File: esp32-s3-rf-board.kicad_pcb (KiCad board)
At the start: 4 copper layers, 50 x 40 mm, 26 parts, among them J1 USB-C 16P, J2 u.FL, J3 UART_4P, J4 I2C_4P, J5 SPI_6P, SW1 RST_BTN, SW2 BOOT_BTN, U1 ESP32-S3-WROOM, U2 AP2112K-3.3V, U3 CP2102-GMR

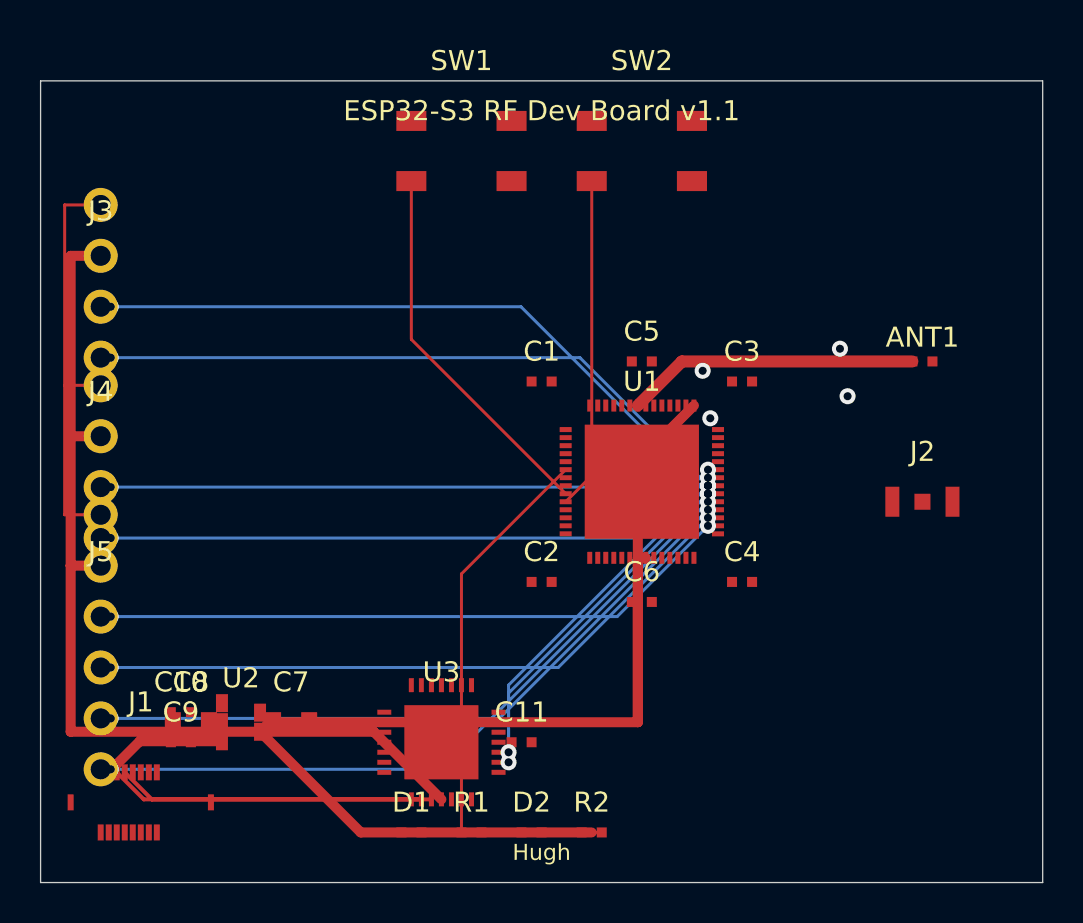
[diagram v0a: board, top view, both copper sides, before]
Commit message: v1.2: 40 MHz crystal, ESP32-S3FN8 flash, real schematic
Closes the three fab-blockers for the bare QFN56 design. Adds Y1
(40 MHz NX3225GA) with C12/C13 12 pF NP0 load caps on XTAL_P/XTAL_N,
swaps U1 to ESP32-S3FN8 (8 MB internal flash, same QFN56 footprint),
and replaces the placeholder .kicad_sch with real symbols + nets
(ERC: 0 errors). Also adds EN 10k pull-up (R5), USB 22R series damping
(R6, R7), decaps repositioned within 2 mm of every VDD pad, and the
previously-uncommitted v1.1 USB-C CC / ESD / test-point work in
reroute_clean.py.

Layout cleanup still pending: the auto-generator leaves 135 DRC
violations and 122 unconnected nets (USB-C pads overlapping J5, LDO
near C8, RF keepout around antenna). Manual Pcbnew pass required
before sending Gerbers to JLCPCB.
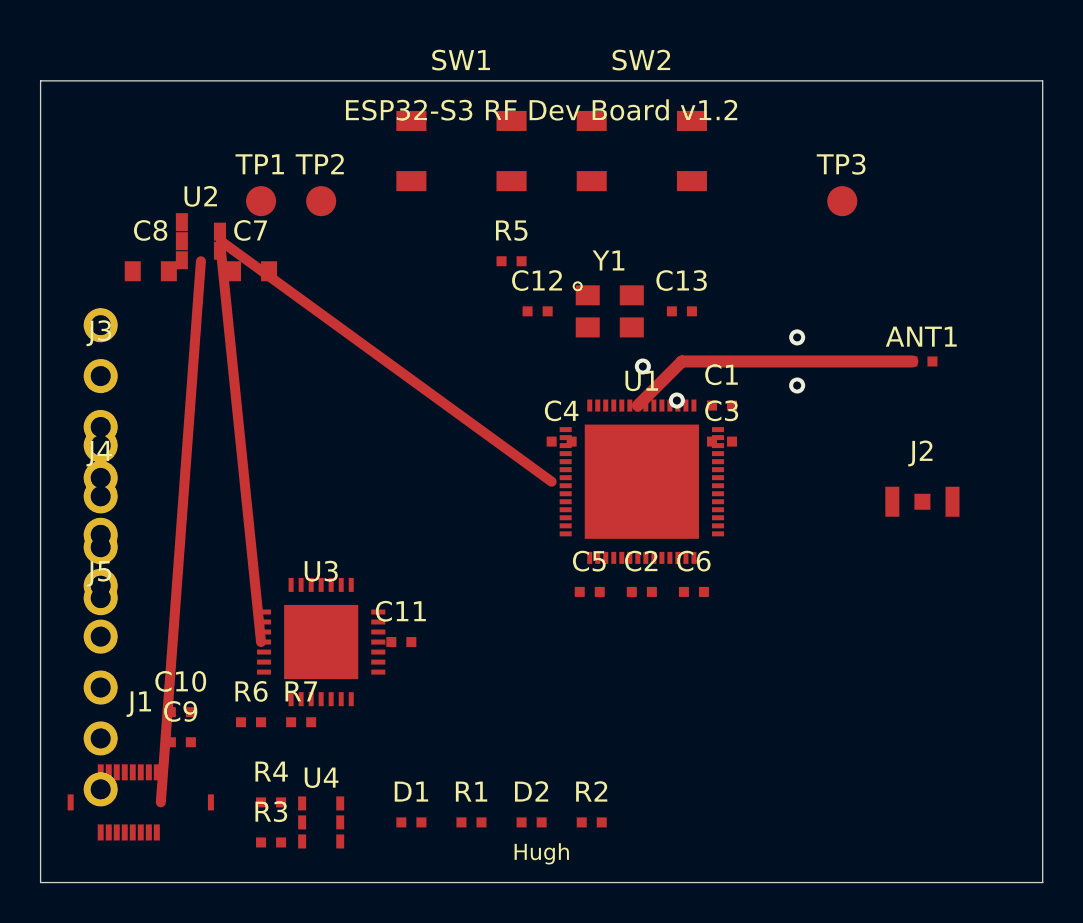
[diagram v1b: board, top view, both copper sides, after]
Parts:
- added C12: 12pF, C12_fp, F.Cu at (24.8, 11.5)
- added C13: 12pF, C13_fp, F.Cu at (32.0, 11.5)
- added R3: 5.1k, R3_fp, F.Cu at (11.5, 38.0)
- added R4: 5.1k, R4_fp, F.Cu at (11.5, 36.0)
- added R5: 10k, R5_fp, F.Cu at (23.5, 9.00)
- added R6: 22R, R6_fp, F.Cu at (10.5, 32.0)
- added R7: 22R, R7_fp, F.Cu at (13.0, 32.0)
- added TP1: TP_3V3, TP1_fp, F.Cu at (11.0, 6.00)
- added TP2: TP_GND, TP2_fp, F.Cu at (14.0, 6.00)
- added TP3: TP_RF, TP3_fp, F.Cu at (40.0, 6.00)
- added U4: USBLC6-2SC6, U4_fp, F.Cu at (14.0, 37.0)
- added Y1: 40MHz, Y1_fp, F.Cu at (28.4, 11.5)
- moved U2 24.1 mm to (8.00, 8.00)
- moved C7 22.6 mm to (10.5, 9.50)
- moved C8 22.6 mm to (5.50, 9.50)
- moved C5 11.8 mm to (27.4, 25.5)
- moved C4 11.4 mm to (26.0, 18.0)
- moved C1 9.08 mm to (34.0, 16.2)
- moved C11 7.81 mm to (18.0, 28.0)
- moved U3 7.81 mm to (14.0, 28.0)
- moved J3 6.00 mm to (3.00, 16.0)
- moved C2 5.02 mm to (30.0, 25.5)
- moved C3 3.16 mm to (34.0, 18.0)
- moved J4 3.00 mm to (3.00, 22.0)
- moved C6 2.65 mm to (32.6, 25.5)
- moved J5 1.00 mm to (3.00, 29.0)
- moved D1 0.50 mm to (18.5, 37.0)
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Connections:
- J1 pad 13: (no net) -> USB_CC2
- J1 pad 5: (no net) -> USB_CC1
- U1 pad 24: (no net) -> I2C_SDA
- U1 pad 25: (no net) -> I2C_SCL
- U1 pad 39: (no net) -> XTAL_P
- U1 pad 40: (no net) -> XTAL_N
- U3 pad 2: USB_DM -> USB_DM_CP
- U3 pad 3: USB_DP -> USB_DP_CP
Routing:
- net 3V3: track 111.4 -> 40.0 mm
- net UART_TX: track 53.2 -> 0.00 mm, vias 4 -> 0
- net UART_RX: track 51.9 -> 0.00 mm, vias 4 -> 0
- net SPI_CS: track 36.3 -> 0.00 mm, vias 2 -> 0
- net SPI_SCK: track 35.1 -> 0.00 mm, vias 2 -> 0
- net SPI_MISO: track 33.9 -> 0.00 mm, vias 2 -> 0
- net SPI_MOSI: track 32.7 -> 0.00 mm, vias 2 -> 0
- net I2C_SCL: track 32.2 -> 0.00 mm, vias 2 -> 0
- net I2C_SDA: track 31.0 -> 0.00 mm, vias 2 -> 0
- net GND: track 20.9 -> 0.00 mm
- net 5V: track 6.29 -> 27.1 mm
- net GPIO48_LED: track 20.3 -> 0.00 mm
- net EN: track 18.8 -> 0.00 mm
- net GPIO0: track 16.5 -> 0.00 mm
- net USB_DP: track 15.9 -> 0.00 mm
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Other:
- board text added: "ESP32-S3 RF Dev Board v1.2"
- board text removed: "ESP32-S3 RF Dev Board v1.1"

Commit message: v1.2: programmatic DRC cleanup -- 144 -> 33 violations, 0 shorts
Fix the structural issues left over from the auto-generator:

- RF trace: narrow fanout from pad 36 (0.25 mm) widening to 0.6 mm once
  clear of adjacent top-row pads, then vertical stub -> 45-deg -> horizontal.
- RF keepout on F.Cu relaxed to copperpour-only (antenna pads and feed
  trace now allowed; In1.Cu and B.Cu still fully blocked).
- Stitching vias: bumped perpendicular offset 1.2 -> 1.8 mm, dropped the
  chip-adjacent segment, skipped vias inside the 5 mm antenna keepout.
- Removed the long diagonal surface power traces from USB-C/LDO that
  cut through unrelated pads; power distribution now relies on the 3V3
  inner plane + short stubs (to be routed in Pcbnew).
- Relocated footprints: USB-C to (25, 37) so J5 SPI header no longer
  overlaps its pads; headers spread to J3=y6, J4=y17, J5=(8, 25) so no
  THT pad pair is within 1.7 mm; C8 moved off U2 pad 3; C11 offset
  right of U3 pad 11; decaps C3/C4 moved clear of U1 pads 26/27/44/45.
- SOT-23-5 pad 0.6x0.9 -> 0.55x0.8 so intra-footprint clearance passes
  the 0.1 mm rule.
- POWER netclass clearance 0.15 -> 0.1 mm (matches default).
- allow_soldermask_bridges_in_footprints: yes.

Final state: 0 shorts, 0 clearance, 0 keepout, 0 hole-clearance errors.
Remaining 33 are courtyard/silk/dangling-via warnings. 120 unconnected
nets still need a Pcbnew routing pass before Gerber export.
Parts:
- moved C10 20.0 mm to (27.0, 32.5)
- moved C9 20.0 mm to (27.0, 34.0)
- moved J1 20.0 mm to (25.0, 37.0)
- moved D1 20.0 mm to (38.5, 37.0)
- moved R1 20.0 mm to (41.5, 37.0)
- moved D2 19.0 mm to (43.5, 37.0)
- moved R2 19.0 mm to (46.5, 37.0)
- moved R4 18.5 mm to (30.0, 35.0)
- moved J3 10.0 mm to (3.00, 6.00)
- moved R3 9.01 mm to (20.0, 35.0)
- moved J5 6.40 mm to (8.00, 25.0)
- moved J4 5.00 mm to (3.00, 17.0)
- moved U4 4.00 mm to (18.0, 37.0)
- moved C8 2.06 mm to (6.00, 11.5)
- moved C3 1.50 mm to (35.5, 18.0)
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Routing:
- net 3V3: track 40.0 -> 0.00 mm
- net 5V: track 27.1 -> 0.00 mm
- net RF_ANT: track 14.6 -> 15.5 mm
- net GND: vias 4 -> 2
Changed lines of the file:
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@@
     (pad_to_mask_clearance 0.05)
     (solder_mask_min_width 0.05)
-    (allow_soldermask_bridges_in_footprints no)
+    (allow_soldermask_bridges_in_footprints yes)
     (pcbplotparams
       (layerselection 0x00010fc_ffffffff)
@@
     (fp_line (start 1.5 1.4) (end -1.5 1.4) (layer "F.Fab") (stroke (width 0.1) (type solid)))
     (fp_line (start -1.5 1.4) (end -1.5 -1.4) (layer "F.Fab") (stroke (width 0.1) (type solid)))
-    (pad "1" smd rect (at -0.95 -0.95) (size 0.6 0.9) (layers "F.Cu" "F.Paste" "F.Mask") (net 16 "EN"))
-    (pad "2" smd rect (at -0.95 0) (size 0.6 0.9) (layers "F.Cu" "F.Paste" "F.Mask") (net 1 "GND"))
-    (pad "3" smd rect (at -0.95 0.95) (size 0.6 0.9) (layers "F.Cu" "F.Paste" "F.Mask") (net 3 "5V"))
-    (pad "4" smd rect (at 0.95 -0.475) (size 0.6 0.9) (layers "F.Cu" "F.Paste" "F.Mask"))
-    (pad "5" smd rect (at 0.95 0.475) (size 0.6 0.9) (layers "F.Cu" "F.Paste" "F.Mask") (net 2 "3V3"))
+    (pad "1" smd rect (at -0.95 -0.95) (size 0.55 0.8) (layers "F.Cu" "F.Paste" "F.Mask") (net 16 "EN"))
+    (pad "2" smd rect (at -0.95 0) (size 0.55 0.8) (layers "F.Cu" "F.Paste" "F.Mask") (net 1 "GND"))
+    (pad "3" smd rect (at -0.95 0.95) (size 0.55 0.8) (layers "F.Cu" "F.Paste" "F.Mask") (net 3 "5V"))
+    (pad "4" smd rect (at 0.95 -0.475) (size 0.55 0.8) (layers "F.Cu" "F.Paste" "F.Mask"))
+    (pad "5" smd rect (at 0.95 0.475) (size 0.55 0.8) (layers "F.Cu" "F.Paste" "F.Mask") (net 2 "3V3"))
   )
   (footprint "J1_fp" (layer "F.Cu")
-    (at 5 36)
+    (at 25 37)
     (attr smd)
     (fp_text reference "J1" (at 0 -5) (layer "F.SilkS")
@@
   )
   (footprint "J3_fp" (layer "F.Cu")
-    (at 3 16)
+    (at 3 6)
     (fp_text reference "J3" (at 0 -3.5) (layer "F.SilkS")
       (effects (font (size 1 1) (thickness 0.15))))
@@
   )
   (footprint "J4_fp" (layer "F.Cu")
-    (at 3 22)
+    (at 3 17)
     (fp_text reference "J4" (at 0 -3.5) (layer "F.SilkS")
       (effects (font (size 1 1) (thickness 0.15))))
@@
   )
   (footprint "J5_fp" (layer "F.Cu")
-    (at 3 29)
+    (at 8 25)
     (fp_text reference "J5" (at 0 -4.5) (layer "F.SilkS")
       (effects (font (size 1 1) (thickness 0.15))))
@@
   )
   (footprint "D1_fp" (layer "F.Cu")
-    (at 18.5 37)
+    (at 38.5 37)
     (attr smd)
     (fp_text reference "D1" (at 0 -1.5) (layer "F.SilkS")
@@
   )
   (footprint "D2_fp" (layer "F.Cu")
-    (at 24.5 37)
+    (at 43.5 37)
     (attr smd)
     (fp_text reference "D2" (at 0 -1.5) (layer "F.SilkS")
@@
   )
   (footprint "R1_fp" (layer "F.Cu")
-    (at 21.5 37)
+    (at 41.5 37)
     (attr smd)
     (fp_text reference "R1" (at 0 -1.5) (layer "F.SilkS")
@@
   )
   (footprint "R2_fp" (layer "F.Cu")
-    (at 27.5 37)
+    (at 46.5 37)
     (attr smd)
     (fp_text reference "R2" (at 0 -1.5) (layer "F.SilkS")
@@
   )
   (footprint "R3_fp" (layer "F.Cu")
-    (at 11.5 38)
+    (at 20 35)
     (attr smd)
     (fp_text reference "R3" (at 0 -1.5) (layer "F.SilkS")
@@
   )
   (footprint "R4_fp" (layer "F.Cu")
-    (at 11.5 36)
+    (at 30 35)
     (attr smd)
     (fp_text reference "R4" (at 0 -1.5) (layer "F.SilkS")
@@
   )
   (footprint "U4_fp" (layer "F.Cu")
-    (at 14 37)
+    (at 18 37)
     (attr smd)
     (fp_text reference "U4" (at 0 -2.2) (layer "F.SilkS")
@@
   )
   (footprint "C3_fp" (layer "F.Cu")
-    (at 34 18)
+    (at 35.5 18)
     (attr smd)
     (fp_text reference "C3" (at 0 -1.5) (layer "F.SilkS")
@@
   )
   (footprint "C4_fp" (layer "F.Cu")
-    (at 26 18)
+    (at 24.5 18)
     (attr smd)
     (fp_text reference "C4" (at 0 -1.5) (layer "F.SilkS")
@@
   )
   (footprint "C7_fp" (layer "F.Cu")
-    (at 10.5 9.5)
+    (at 11.5 10.5)
     (attr smd)
     (fp_text reference "C7" (at 0 -2) (layer "F.SilkS")
@@
   )
   (footprint "C8_fp" (layer "F.Cu")
-    (at 5.5 9.5)
+    (at 6 11.5)
     (attr smd)
     (fp_text reference "C8" (at 0 -2) (layer "F.SilkS")
@@
   )
   (footprint "C9_fp" (layer "F.Cu")
-    (at 7 33)
+    (at 27 34)
     (attr smd)
     (fp_text reference "C9" (at 0 -1.5) (layer "F.SilkS")
@@
   )
   (footprint "C10_fp" (layer "F.Cu")
-    (at 7 31.5)
+    (at 27 32.5)
     (attr smd)
     (fp_text reference "C10" (at 0 -1.5) (layer "F.SilkS")
@@
   )
   (footprint "C11_fp" (layer "F.Cu")
-    (at 18 28)
+    (at 18.5 28)
     (attr smd)
     (fp_text reference "C11" (at 0 -1.5) (layer "F.SilkS")
@@
     (pad "2" smd rect (at 0.5 0) (size 0.5 0.5) (layers "F.Cu" "F.Paste" "F.Mask") (net 1 "GND"))
   )
-  (segment (start 29.8 16.2) (end 32 14) (width 0.6) (layer "F.Cu") (net 4))
-  (segment (start 32 14) (end 43.5 14) (width 0.6) (layer "F.Cu") (net 4))
-  (via (at 31.7485 15.9485) (size 0.8) (drill 0.4) (layers "F.Cu" "B.Cu") (net 1))
-  (via (at 30.0515 14.2515) (size 0.8) (drill 0.4) (layers "F.Cu" "B.Cu") (net 1))
-  (via (at 37.75 15.2) (size 0.8) (drill 0.4) (layers "F.Cu" "B.Cu") (net 1))
-  (via (at 37.75 12.8) (size 0.8) (drill 0.4) (layers "F.Cu" "B.Cu") (net 1))
-  (segment (start 6 36) (end 8 9) (width 0.5) (layer "F.Cu") (net 3))
-  (segment (start 9 8) (end 25.5 20) (width 0.5) (layer "F.Cu") (net 2))
-  (segment (start 9 8.5) (end 11 28) (width 0.5) (layer "F.Cu") (net 2))
+  (segment (start 29.8 16.2) (end 29.8 15.3) (width 0.25) (layer "F.Cu") (net 4))
+  (segment (start 29.8 15.3) (end 29.8 14.6) (width 0.6) (layer "F.Cu") (net 4))
+  (segment (start 29.8 14.6) (end 30.4 14) (width 0.6) (layer "F.Cu") (net 4))
+  (segment (start 30.4 14) (end 43.5 14) (width 0.6) (layer "F.Cu") (net 4))
+  (via (at 33.675 15.8) (size 0.8) (drill 0.4) (layers "F.Cu" "B.Cu") (net 1))
+  (via (at 33.675 12.2) (size 0.8) (drill 0.4) (layers "F.Cu" "B.Cu") (net 1))
   (zone (net 1) (net_name "GND") (layer "In1.Cu") (name "GND_PLANE")
     (hatch edge 0.508)
@@
   (zone (net 0) (net_name "") (layer "F.Cu") (name "RF_KEEPOUT")
     (hatch edge 0.508)
-    (keepout (tracks not_allowed) (vias not_allowed) (pads not_allowed) (copperpour not_allowed) (footprints allowed))
+    (keepout (tracks allowed) (vias allowed) (pads allowed) (copperpour not_allowed) (footprints allowed))
     (polygon
       (pts
